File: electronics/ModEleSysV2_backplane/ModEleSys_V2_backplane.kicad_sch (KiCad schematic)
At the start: 40 parts, among them J13 Conn_01x03, J15 Conn_01x03, J5 Conn_01x03, J6 Conn_01x03, J7 Conn_01x03, J8 Conn_01x03, SW1 switch_DPDT, SW2 switch_DPDT

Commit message: updated backplane with 2x3 XH connectors
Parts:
- removed J13, J15, J7, J8: Conn_01x03, Connector_JST:JST_PH_B3B-PH-K_1x03_P2.00mm_Vertical, symbol Connector_Generic:Conn_01x03
- added J7, J9: Conn_02x03_Odd_Even, symbol Connector_Generic:Conn_02x03_Odd_Even
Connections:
- net at SW1.1 (SW1_P1): now also J7.1 (Pin_1)
- net at SW1.2 (SW1_C1): now also J7.3 (Pin_3)
- net at SW1.3 (SW1_P2): now also J7.5 (Pin_5)
- net at SW1.4 (SW2_P2): now also J7.6 (Pin_6)
- net at SW1.5 (SW2_C1): now also J7.4 (Pin_4)
- net at SW1.6 (SW2_P2): now also J7.2 (Pin_2)
- net at SW2.3 (SW1_P2): now also J9.5 (Pin_5)
- net at SW2.2 (SW1_C1): now also J9.3 (Pin_3)
- net at SW2.1 (SW1_P1): now also J9.1 (Pin_1)
- net at SW2.4 (SW2_P2): now also J9.6 (Pin_6)
- net at SW2.5 (SW2_C1): now also J9.4 (Pin_4)
- net at SW2.6 (SW2_P2): now also J9.2 (Pin_2)
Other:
- moved on the sheet: SW1, SW2

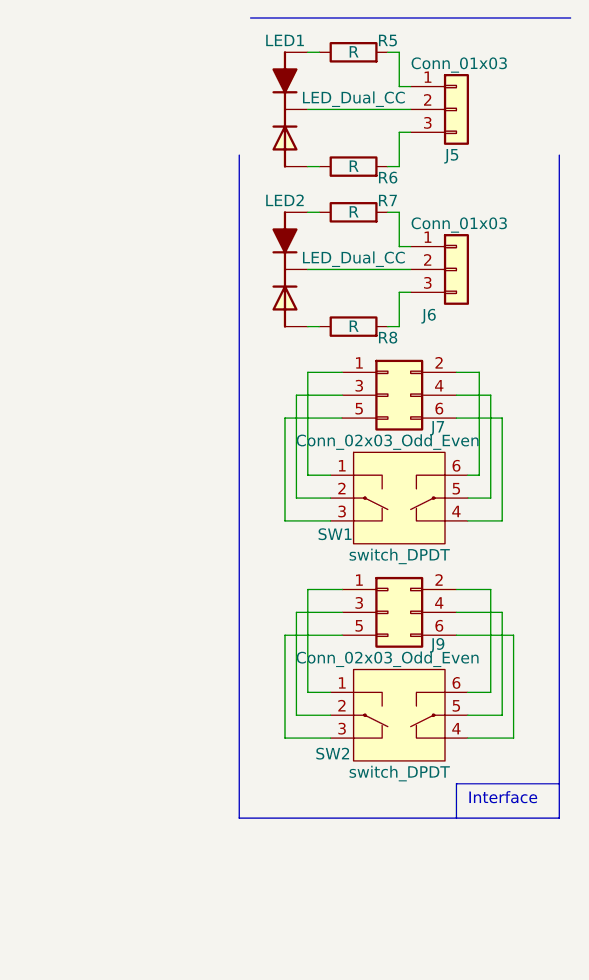
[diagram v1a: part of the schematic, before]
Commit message: changed power on/off connector on backplane
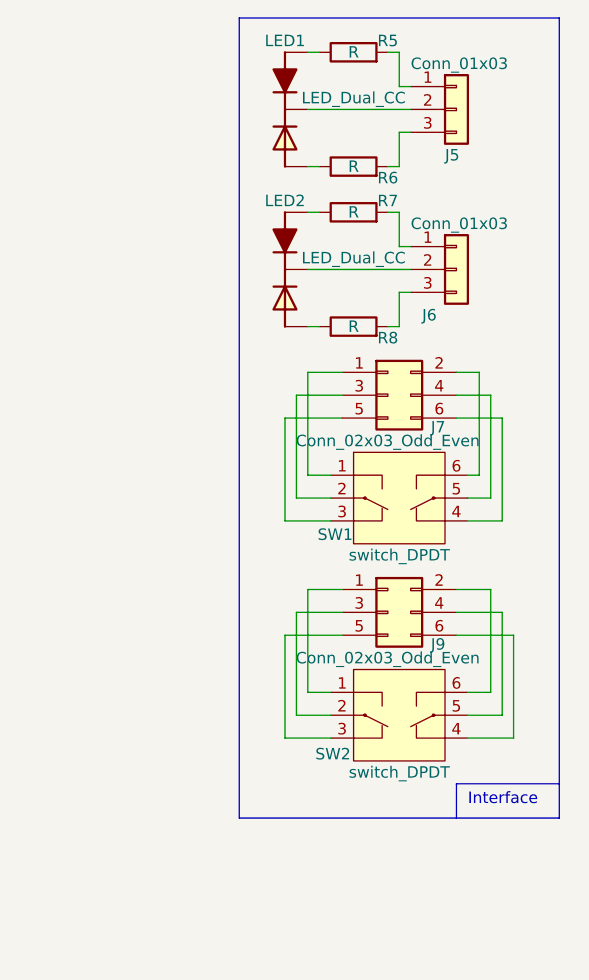
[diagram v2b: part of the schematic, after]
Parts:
- J7, J9: footprint (none) -> SquantorConnectors:DLL-XHY-6A
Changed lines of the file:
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@@
 	(polyline
 		(pts
-			(xy 280.67 104.14) (xy 280.67 30.48)
+			(xy 280.67 104.14) (xy 280.67 15.24)
 		)
 		(stroke
@@
 	(polyline
 		(pts
-			(xy 245.11 30.48) (xy 245.11 104.14)
+			(xy 245.11 15.24) (xy 245.11 104.14)
 		)
 		(stroke
@@
 	(polyline
 		(pts
-			(xy 281.94 15.24) (xy 246.38 15.24)
+			(xy 280.67 15.24) (xy 245.11 15.24)
 		)
 		(stroke
@@
 			)
 		)
-		(property "Footprint" ""
+		(property "Footprint" "SquantorConnectors:DLL-XHY-6A"
 			(at 261.62 57.15 0)
 			(effects
@@
 			)
 		)
-		(property "Footprint" ""
+		(property "Footprint" "SquantorConnectors:DLL-XHY-6A"
 			(at 261.62 81.28 0)
 			(effects
